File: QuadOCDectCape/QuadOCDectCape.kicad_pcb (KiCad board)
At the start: 2 copper layers, 54.6 x 119.9 mm, 31 parts, among them IC1 MCT6H, IC2 MCT6H, IC3 MCT6H, IC4 MCT6H, P8 BeagleBone_Black_Header, P9 BeagleBone_Black_Header, T1 In Track1 Out, T2 In Track2 Out, T3 In Track3 Out, T4 In Track4 Out, U1 CAT24C256W

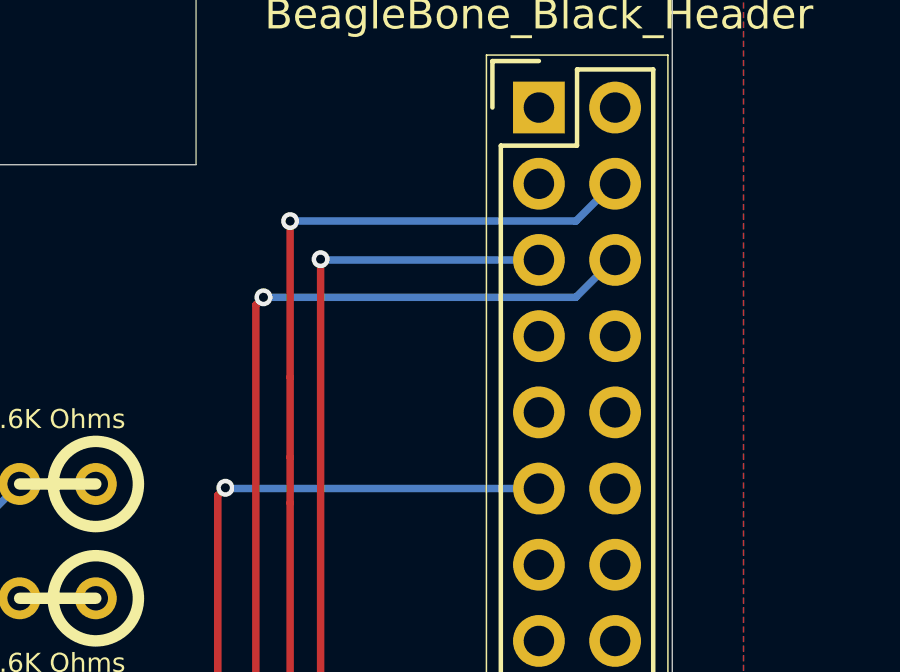
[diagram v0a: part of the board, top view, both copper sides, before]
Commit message: Update QuadOCDectCape to correct GPIO conflict with QuadSMCSenseCape
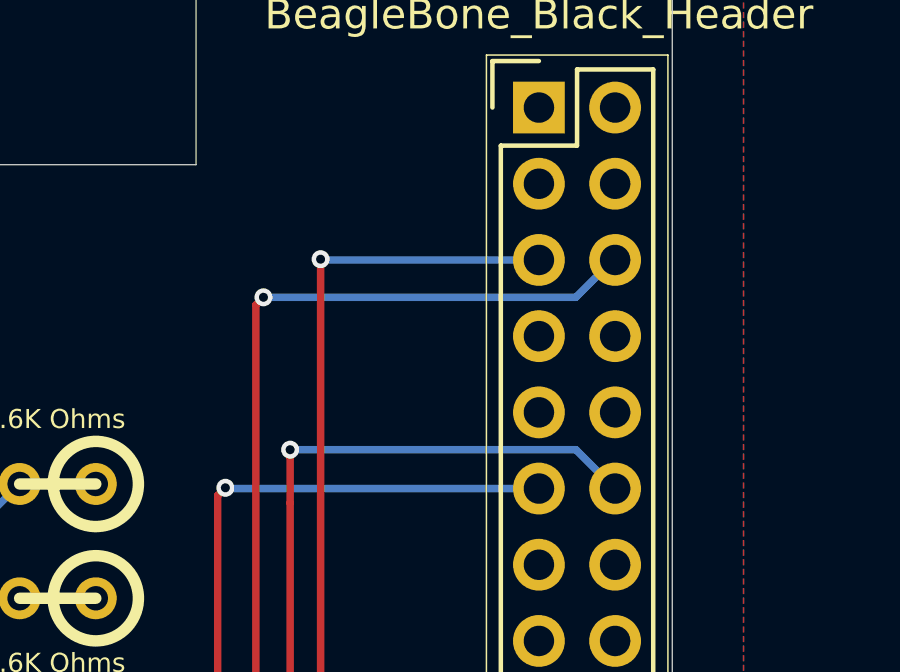
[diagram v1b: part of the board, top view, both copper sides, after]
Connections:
- P8 pad 12: (no net) -> /Occupancy Detector 1/OD1
- P8 pad 4: /Occupancy Detector 1/OD1 -> (no net)
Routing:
- net /Occupancy Detector 1/OD1: track 91.5 -> 83.9 mm
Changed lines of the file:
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@@
     (thickness 1.6)
     (drawings 9)
-    (tracks 175)
+    (tracks 174)
     (zones 0)
     (modules 31)
@@
     (pad 4 thru_hole oval (at 2.54 2.54) (size 1.7272 1.7272) (drill 1.016)
       (layers *.Cu *.Mask F.SilkS)
+    )
+    (pad 5 thru_hole oval (at 0 5.08) (size 1.7272 1.7272) (drill 1.016)
+      (layers *.Cu *.Mask F.SilkS)
+      (net 6 "/Occupancy Detector 2/OD2")
+    )
+    (pad 6 thru_hole oval (at 2.54 5.08) (size 1.7272 1.7272) (drill 1.016)
+      (layers *.Cu *.Mask F.SilkS)
+      (net 7 "/Occupancy Detector 3/OD3")
+    )
+    (pad 7 thru_hole oval (at 0 7.62) (size 1.7272 1.7272) (drill 1.016)
+      (layers *.Cu *.Mask F.SilkS)
+    )
+    (pad 8 thru_hole oval (at 2.54 7.62) (size 1.7272 1.7272) (drill 1.016)
+      (layers *.Cu *.Mask F.SilkS)
+    )
+    (pad 9 thru_hole oval (at 0 10.16) (size 1.7272 1.7272) (drill 1.016)
+      (layers *.Cu *.Mask F.SilkS)
+    )
+    (pad 10 thru_hole oval (at 2.54 10.16) (size 1.7272 1.7272) (drill 1.016)
+      (layers *.Cu *.Mask F.SilkS)
+    )
+    (pad 11 thru_hole oval (at 0 12.7) (size 1.7272 1.7272) (drill 1.016)
+      (layers *.Cu *.Mask F.SilkS)
+      (net 8 "/Occupancy Detector 4/OD4")
+    )
+    (pad 12 thru_hole oval (at 2.54 12.7) (size 1.7272 1.7272) (drill 1.016)
+      (layers *.Cu *.Mask F.SilkS)
       (net 5 "/Occupancy Detector 1/OD1")
-    )
-    (pad 5 thru_hole oval (at 0 5.08) (size 1.7272 1.7272) (drill 1.016)
-      (layers *.Cu *.Mask F.SilkS)
-      (net 6 "/Occupancy Detector 2/OD2")
-    )
-    (pad 6 thru_hole oval (at 2.54 5.08) (size 1.7272 1.7272) (drill 1.016)
-      (layers *.Cu *.Mask F.SilkS)
-      (net 7 "/Occupancy Detector 3/OD3")
-    )
-    (pad 7 thru_hole oval (at 0 7.62) (size 1.7272 1.7272) (drill 1.016)
-      (layers *.Cu *.Mask F.SilkS)
-    )
-    (pad 8 thru_hole oval (at 2.54 7.62) (size 1.7272 1.7272) (drill 1.016)
-      (layers *.Cu *.Mask F.SilkS)
-    )
-    (pad 9 thru_hole oval (at 0 10.16) (size 1.7272 1.7272) (drill 1.016)
-      (layers *.Cu *.Mask F.SilkS)
-    )
-    (pad 10 thru_hole oval (at 2.54 10.16) (size 1.7272 1.7272) (drill 1.016)
-      (layers *.Cu *.Mask F.SilkS)
-    )
-    (pad 11 thru_hole oval (at 0 12.7) (size 1.7272 1.7272) (drill 1.016)
-      (layers *.Cu *.Mask F.SilkS)
-      (net 8 "/Occupancy Detector 4/OD4")
-    )
-    (pad 12 thru_hole oval (at 2.54 12.7) (size 1.7272 1.7272) (drill 1.016)
-      (layers *.Cu *.Mask F.SilkS)
     )
     (pad 13 thru_hole oval (at 0 15.24) (size 1.7272 1.7272) (drill 1.016)
@@
   (segment (start 143.51 85.09) (end 143.383 85.217) (width 0.25) (layer F.Cu) (net 4))
   (segment (start 143.51 78.74) (end 147.32 78.74) (width 0.25) (layer B.Cu) (net 4))
+  (segment (start 167.1701 75.0824) (end 167.1574 75.0824) (width 0.25) (layer B.Cu) (net 5))
+  (via (at 156.337 73.787) (size 0.6) (layers F.Cu B.Cu) (net 5))
+  (segment (start 165.862 73.787) (end 156.337 73.787) (width 0.25) (layer B.Cu) (net 5))
+  (segment (start 167.1574 75.0824) (end 165.862 73.787) (width 0.25) (layer B.Cu) (net 5))
   (segment (start 156.337 75.565) (end 156.337 92.456) (width 0.25) (layer F.Cu) (net 5))
-  (segment (start 167.1066 64.9224) (end 165.862 66.167) (width 0.25) (layer B.Cu) (net 5))
-  (segment (start 165.862 66.167) (end 156.337 66.167) (width 0.25) (layer B.Cu) (net 5))
-  (via (at 156.337 66.167) (size 0.6) (layers F.Cu B.Cu) (net 5))
-  (segment (start 156.337 66.167) (end 156.337 71.374) (width 0.25) (layer F.Cu) (net 5))
-  (segment (start 156.337 71.374) (end 156.337 74.041) (width 0.25) (layer F.Cu) (net 5))
+  (segment (start 156.337 73.787) (end 156.337 74.041) (width 0.25) (layer F.Cu) (net 5))
   (segment (start 156.337 74.041) (end 156.337 75.565) (width 0.25) (layer F.Cu) (net 5))
-  (segment (start 167.1701 64.9224) (end 167.1066 64.9224) (width 0.25) (layer B.Cu) (net 5))
   (segment (start 129.54 110.49) (end 133.35 110.49) (width 0.25) (layer B.Cu) (net 5))
   (via (at 129.54 110.49) (size 0.6) (layers F.Cu B.Cu) (net 5))

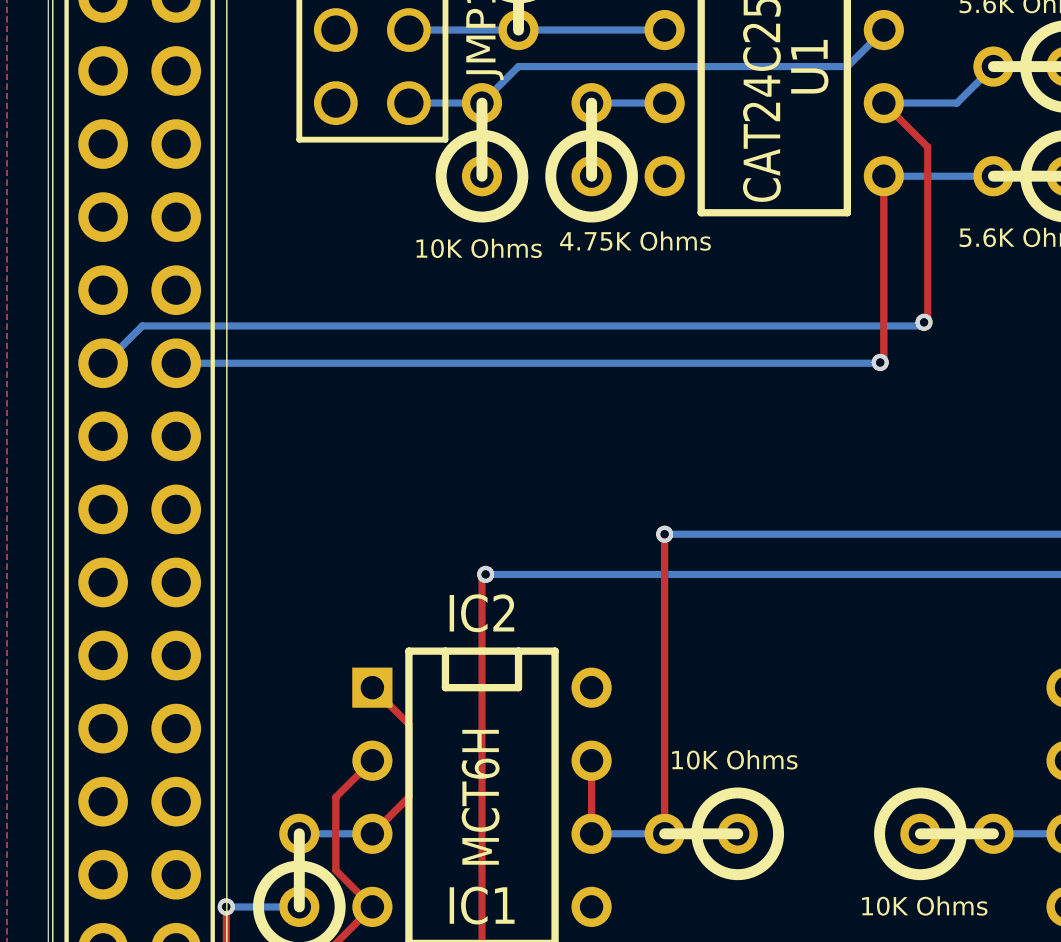
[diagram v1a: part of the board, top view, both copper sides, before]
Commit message: Add serial pass-through header to QuadOCDectCape.
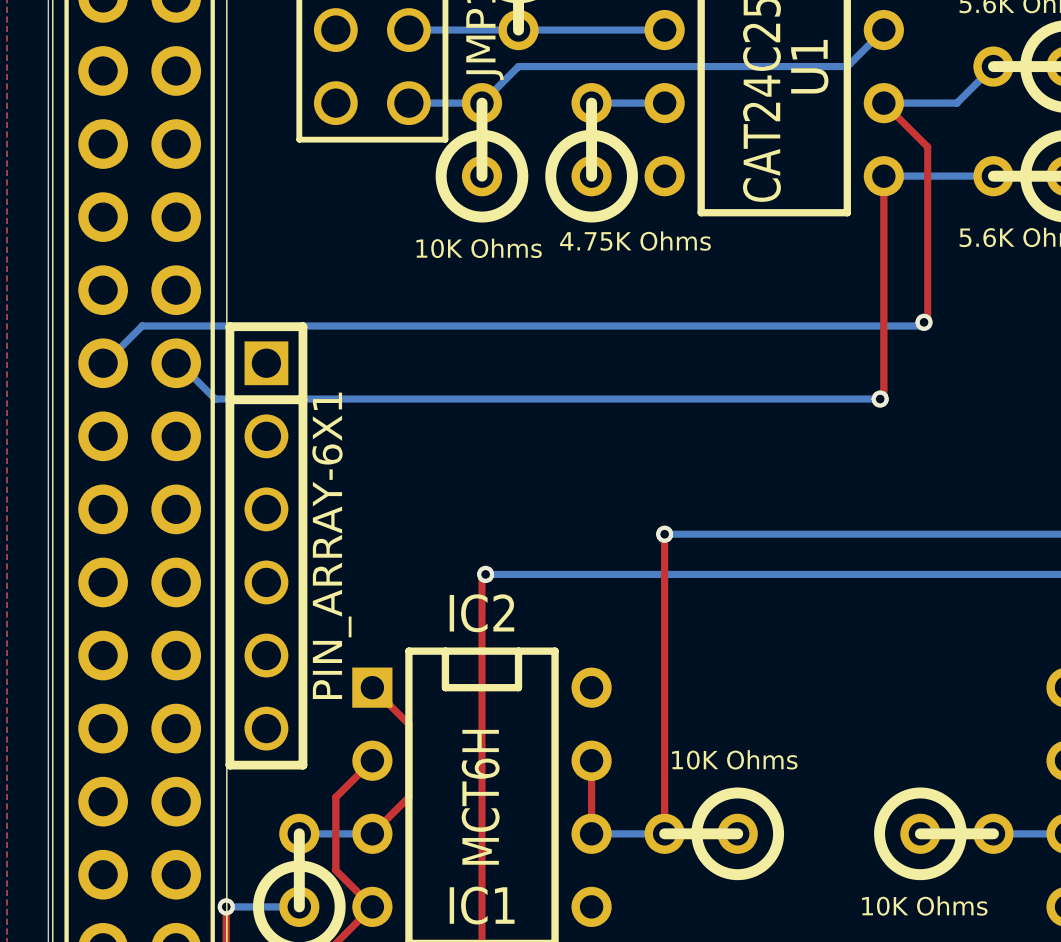
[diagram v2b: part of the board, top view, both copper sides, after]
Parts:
- added PIN_ARRAY-6X1: Val**, PIN_ARRAY-6X1, F.Cu at (122.0, 91.6)
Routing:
- net /Cape EEProm/SDA: track 34.8 -> 36.8 mm
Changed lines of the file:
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@@
   (general
     (links 90)
-    (no_connects 0)
+    (no_connects 33)
     (area 103.317323 40.64 177.682877 163.830001)
     (thickness 1.6)
     (drawings 9)
-    (tracks 174)
+    (tracks 177)
     (zones 0)
-    (modules 31)
+    (modules 32)
     (nets 31)
   )
@@
     )
   )
+  (module PIN_ARRAY-6X1 (layer F.Cu)
+    (at 122.047 91.5924 270)
+    (descr "Connecteur 6 pins")
+    (tags "CONN DEV")
+    (fp_text reference PIN_ARRAY-6X1 (at 0 -2.159 270) (layer F.SilkS)
+      (effects (font (size 1.016 1.016) (thickness 0.2032)))
+    )
+    (fp_text value Val** (at 0 2.159 270) (layer F.SilkS) hide
+      (effects (font (size 1.016 0.889) (thickness 0.2032)))
+    )
+    (fp_line (start -7.62 1.27) (end -7.62 -1.27) (layer F.SilkS) (width 0.3048))
+    (fp_line (start -7.62 -1.27) (end 7.62 -1.27) (layer F.SilkS) (width 0.3048))
+    (fp_line (start 7.62 -1.27) (end 7.62 1.27) (layer F.SilkS) (width 0.3048))
+    (fp_line (start 7.62 1.27) (end -7.62 1.27) (layer F.SilkS) (width 0.3048))
+    (fp_line (start -5.08 1.27) (end -5.08 -1.27) (layer F.SilkS) (width 0.3048))
+    (pad 1 thru_hole rect (at -6.35 0 270) (size 1.524 1.524) (drill 1.016)
+      (layers *.Cu *.Mask F.SilkS)
+    )
+    (pad 2 thru_hole circle (at -3.81 0 270) (size 1.524 1.524) (drill 1.016)
+      (layers *.Cu *.Mask F.SilkS)
+    )
+    (pad 3 thru_hole circle (at -1.27 0 270) (size 1.524 1.524) (drill 1.016)
+      (layers *.Cu *.Mask F.SilkS)
+    )
+    (pad 4 thru_hole circle (at 1.27 0 270) (size 1.524 1.524) (drill 1.016)
+      (layers *.Cu *.Mask F.SilkS)
+    )
+    (pad 5 thru_hole circle (at 3.81 0 270) (size 1.524 1.524) (drill 1.016)
+      (layers *.Cu *.Mask F.SilkS)
+    )
+    (pad 6 thru_hole circle (at 6.35 0 270) (size 1.524 1.524) (drill 1.016)
+      (layers *.Cu *.Mask F.SilkS)
+    )
+    (model pin_array/pins_array_6x1.wrl
+      (at (xyz 0 0 0))
+      (scale (xyz 1 1 1))
+      (rotate (xyz 0 0 0))
+    )
+  )
   (gr_arc (start 120.8151 49.0474) (end 114.4651 49.0474) (angle 90) (layer Edge.Cuts) (width 0.00254))
   (gr_line (start 135.4201 42.6974) (end 120.8151 42.6974) (layer Edge.Cuts) (width 0.00254))
@@
   (segment (start 143.51 76.2) (end 146.05 76.2) (width 0.25) (layer B.Cu) (net 3))
   (segment (start 146.05 76.2) (end 147.32 74.93) (width 0.25) (layer B.Cu) (net 3))
-  (segment (start 143.51 78.74) (end 143.51 85.09) (width 0.25) (layer F.Cu) (net 4))
-  (segment (start 143.3576 85.2424) (end 118.9101 85.2424) (width 0.25) (layer B.Cu) (net 4))
-  (segment (start 143.383 85.217) (end 143.3576 85.2424) (width 0.25) (layer B.Cu) (net 4))
-  (via (at 143.383 85.217) (size 0.6) (layers F.Cu B.Cu) (net 4))
-  (segment (start 143.51 85.09) (end 143.383 85.217) (width 0.25) (layer F.Cu) (net 4))
+  (segment (start 118.9101 85.2424) (end 119.0244 85.2424) (width 0.25) (layer B.Cu) (net 4) (status C00000))
+  (segment (start 143.383 86.487) (end 143.51 86.36) (width 0.25) (layer B.Cu) (net 4))
+  (segment (start 120.269 86.487) (end 143.383 86.487) (width 0.25) (layer B.Cu) (net 4))
+  (segment (start 119.0244 85.2424) (end 120.269 86.487) (width 0.25) (layer B.Cu) (net 4) (status 400000))
+  (segment (start 143.51 78.74) (end 143.51 86.36) (width 0.25) (layer F.Cu) (net 4) (status 400000))
+  (segment (start 143.383 86.487) (end 143.3576 86.5124) (width 0.25) (layer B.Cu) (net 4))
+  (via (at 143.383 86.487) (size 0.6) (layers F.Cu B.Cu) (net 4))
+  (segment (start 143.51 86.36) (end 143.383 86.487) (width 0.25) (layer F.Cu) (net 4))
   (segment (start 143.51 78.74) (end 147.32 78.74) (width 0.25) (layer B.Cu) (net 4))
   (segment (start 167.1701 75.0824) (end 167.1574 75.0824) (width 0.25) (layer B.Cu) (net 5))
